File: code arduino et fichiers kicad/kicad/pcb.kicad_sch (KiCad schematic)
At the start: 34 parts, among them J1 Screw_Terminal_01x04, J2 Screw_Terminal_01x04, J3 Screw_Terminal_01x02, U1 LMC6482, U2 LMC6482, U3 LMC6482

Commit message: pcb yaddi yadda
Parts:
- removed LED1: LED_LEDCHIP-LED0805, LED_SMD:LED_0805_2012Metric_Pad1.15x1.40mm_HandSolder, symbol Arduino_MEGA_2560-Rev3:LED_LEDCHIP-LED0805
- added D4: LED, PCM_SparkFun-LED:LED_0603_1608Metric, symbol PCM_SparkFun-LED:LED
- added TP1, TP2, TP3: TestPoint, TestPoint:TestPoint_THTPad_D1.5mm_Drill0.7mm, symbol Connector:TestPoint
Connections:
- net GND: now also D4.1 (K)
- net T1 sortie: now also TP1.1
- net T2 sortie: now also TP2.1
- net T3 sortie: now also TP3.1
- net at R18.2: now also D4.2 (A)
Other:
- moved on the sheet: J1, J2, J3, R1, R10, R11, R12, R13, R14, R15, R18, R2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

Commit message: version tht pour pas trop haïr notre vie plus tard
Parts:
- removed J2: Screw_Terminal_01x04, Connector_JST:JST_XH_B4B-XH-A_1x04_P2.50mm_Vertical, symbol Connector:Screw_Terminal_01x04
- removed R1, R10, R15: 6.1K, Resistor_SMD:R_0805_2012Metric_Pad1.20x1.40mm_HandSolder, symbol Device:R
- removed digital1, digital2: Conn_01x18_Pin, Connector_PinHeader_2.54mm:PinHeader_1x18_P2.54mm_Vertical, symbol Connector:Conn_01x18_Pin
- added C16, C17, C18: 2 μF, Capacitor_THT:CP_Radial_D5.0mm_P2.50mm, symbol Device:C
- added RV1, RV2, RV3: R_Potentiometer_Trim, Library:trimpot, symbol Device:R_Potentiometer_Trim
- D4: footprint PCM_SparkFun-LED:LED_0603_1608Metric -> LED_THT:LED_D5.0mm
- R11, R12, R13, R14, R18, R2, R3, R4, R5, R6, R7, R8, R9: footprint Resistor_SMD:R_0805_2012Metric_Pad1.20x1.40mm_HandSolder -> Resistor_THT:R_Axial_DIN0207_L6.3mm_D2.5mm_P7.62mm_Horizontal
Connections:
- net +3.3V: no longer R18.1
- net +5V: now also R18.1
- net +8V: now also J3.2 (Pin_2); no longer J3.1 (Pin_1)
- net GND: now also J3.1 (Pin_1), RV1.3, RV2.3, RV3.3; no longer J3.2 (Pin_2)
- net T1 sortie: now also C16.2, RV1.2
- net T2 sortie: now also C17.2, RV2.2
- net T3 sortie: now also C18.2, RV3.2
- net pwmdroite: now also J1.3 (Pin_3)
- net at R2.2, U1.3 (+): now also C16.1, RV1.1
- net at R8.2, U2.3 (+): now also C17.1, RV2.1
- net at R13.2, U3.3 (+): now also C18.1, RV3.1
- no-connect marks 3 -> 1
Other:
- moved on the sheet: J1, J3, R11, R12, R13, R14, R6, R7, R8, R9, TH2, TH3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

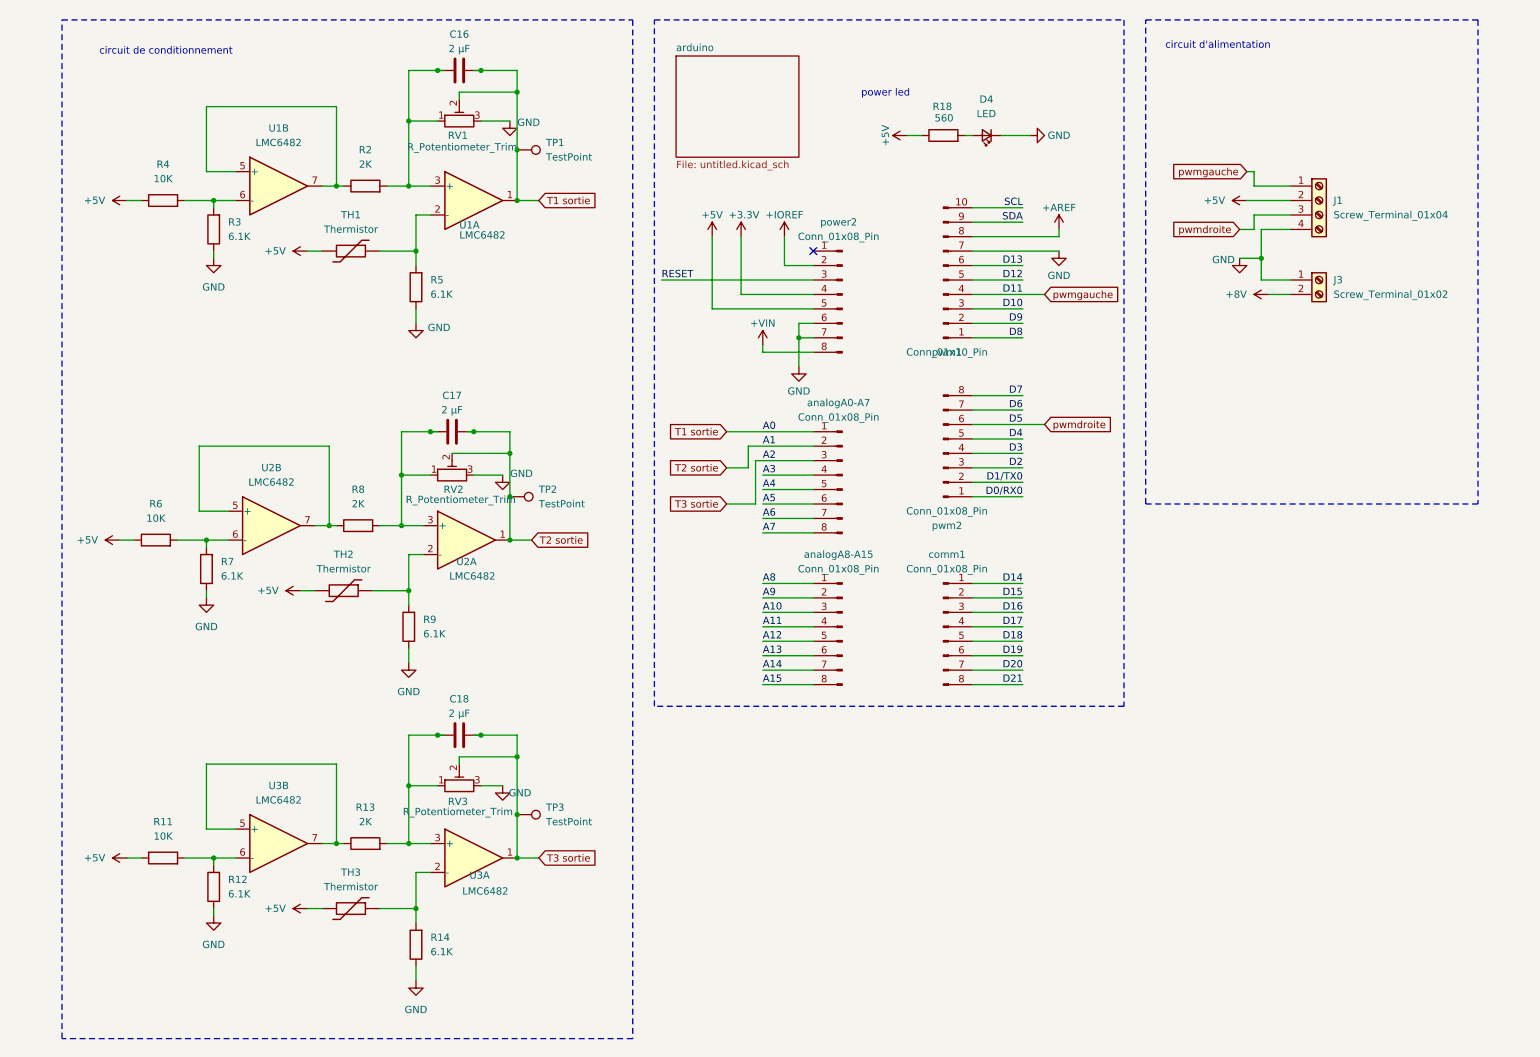
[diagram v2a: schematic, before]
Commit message: Changment connecteur pcb
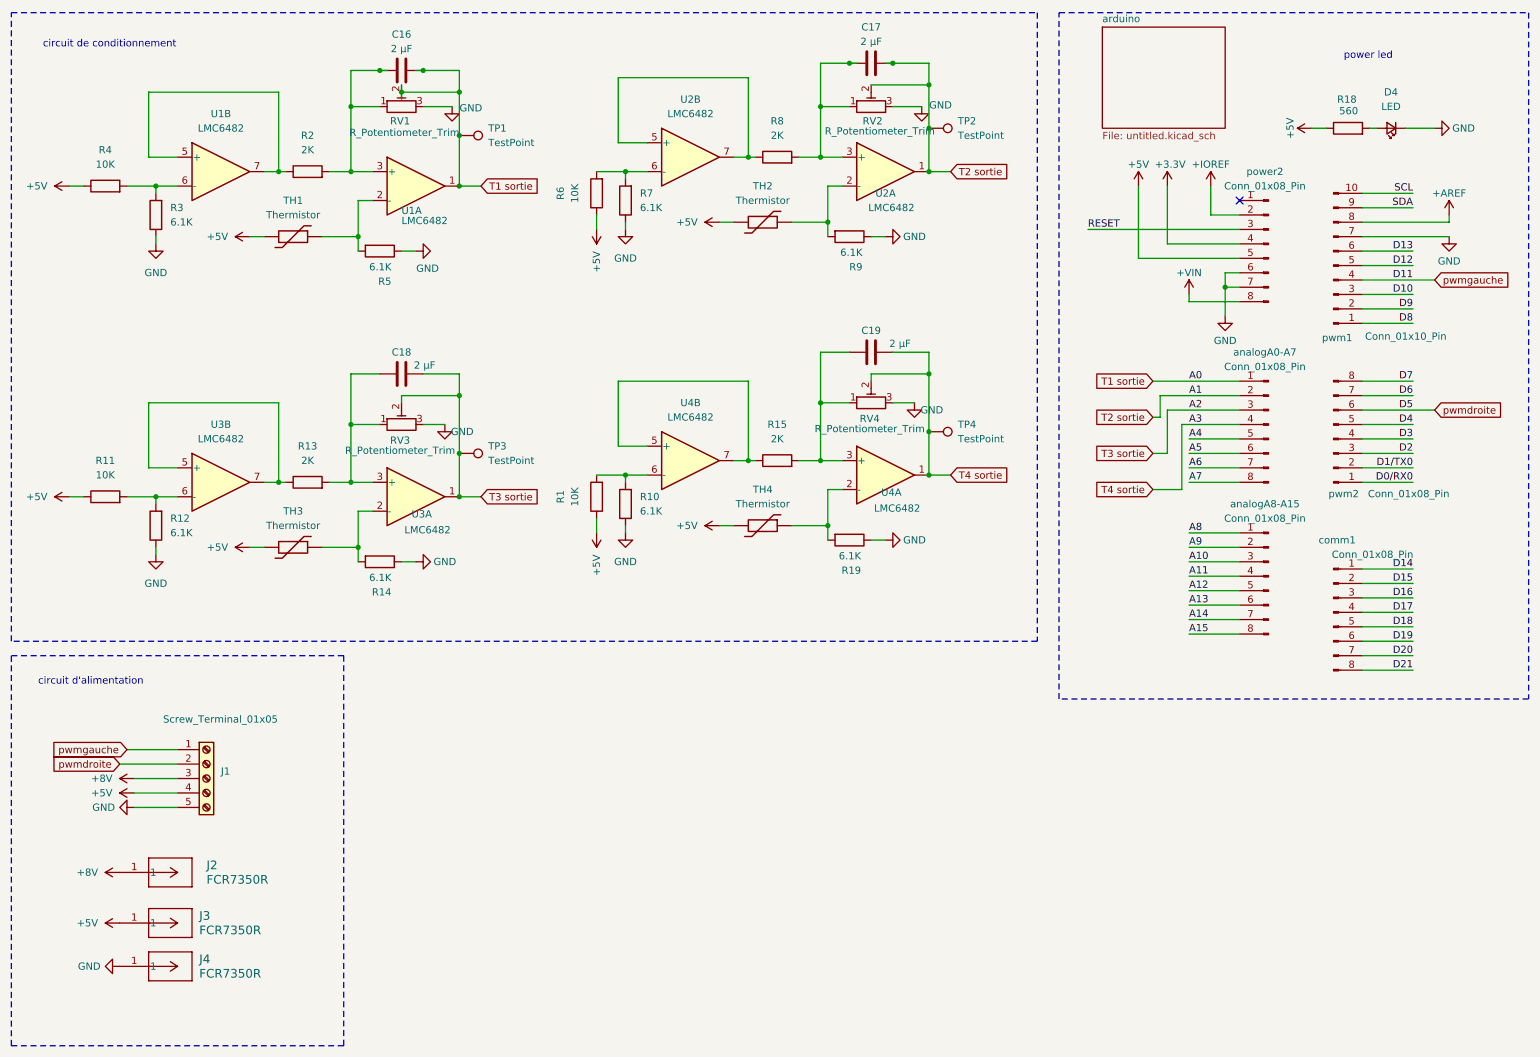
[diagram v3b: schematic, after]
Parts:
- removed J1: Screw_Terminal_01x04, Connector_JST:JST_XH_B4B-XH-A_1x04_P2.50mm_Vertical, symbol Connector:Screw_Terminal_01x04
- removed J3: Screw_Terminal_01x02, Connector_JST:JST_XH_B2B-XH-A_1x02_P2.50mm_Vertical, symbol Connector:Screw_Terminal_01x02
- added C19: 2 μF, Capacitor_THT:CP_Radial_D5.0mm_P2.50mm, symbol Device:C
- added J1: Screw_Terminal_01x05, Connector_JST:JST_XH_B5B-XH-A_1x05_P2.50mm_Vertical, symbol Connector:Screw_Terminal_01x05
- added J2, J3, J4: FCR7350R, CONN1_FCR7350R_CLF, symbol connecteur:FCR7350R
- added R1: 10K, Resistor_THT:R_Axial_DIN0207_L6.3mm_D2.5mm_P7.62mm_Horizontal, symbol Device:R
- added R10, R19: 6.1K, Resistor_THT:R_Axial_DIN0207_L6.3mm_D2.5mm_P7.62mm_Horizontal, symbol Device:R
- added R15: 2K, Resistor_THT:R_Axial_DIN0207_L6.3mm_D2.5mm_P7.62mm_Horizontal, symbol Device:R
- added RV4: R_Potentiometer_Trim, Library:trimpot, symbol Device:R_Potentiometer_Trim
- added TH4: Thermistor, Connector_JST:JST_XH_B2B-XH-A_1x02_P2.50mm_Vertical, symbol Device:Thermistor
- added TP4: TestPoint, TestPoint:TestPoint_THTPad_D1.5mm_Drill0.7mm, symbol Connector:TestPoint
- added U4: LMC6482, ampli op:LMC6482, symbol Amplifier_Operational:LMC6482
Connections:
- net +5V: now also J1.4 (Pin_4), J3.1, R1.1, TH4.2
- net +8V: now also J1.3 (Pin_3), J2.1
- net GND: now also J1.5 (Pin_5), J4.1, R10.1, R19.1, RV4.3
- net pwmdroite: now also J1.2 (Pin_2)
- net pwmgauche: now also J1.1 (Pin_1)
- net A3 renamed T4 sortie
- net T4 sortie: now also C19.2, RV4.2, TP4.1, U4.1
- new net: C19.1, R15.2, RV4.1, U4.3 (+)
- new net: R15.1, U4.5 (+), U4.7
- new net: R1.2, R10.2, U4.6 (-)
- new net: R19.2, TH4.1, U4.2 (-)
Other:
- moved on the sheet: C16, C17, C18, D4, R11, R12, R13, R14, R18, R2, R3, R4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

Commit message: Pcb quasi fini
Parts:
- C16, C17, C18, C19: footprint Capacitor_THT:CP_Radial_D5.0mm_P2.50mm -> Library:condensateur 1uF
- R1, R10, R11, R12, R13, R14, R15, R18, R19, R2, R3, R4, R5, R6, R7, R8, R9: footprint Resistor_THT:R_Axial_DIN0207_L6.3mm_D2.5mm_P7.62mm_Horizontal -> Library:Resistance SMT
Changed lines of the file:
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@@
 	)
 	(junction
-		(at 170.18 22.86)
-		(diameter 0)
-		(color 0 0 0 0)
-	)
-	(junction
 		(at 62.23 41.91)
 		(diameter 0)
@@
 	)
 	(junction
-		(at 80.01 24.13)
-		(diameter 0)
-		(color 0 0 0 0)
-	)
-	(junction
 		(at 74.93 96.52)
 		(diameter 0)
@@
 	)
 	(junction
-		(at 162.56 22.86)
-		(diameter 0)
-		(color 0 0 0 0)
-	)
-	(junction
 		(at 40.64 99.06)
 		(diameter 0)
@@
 	)
 	(junction
-		(at 87.63 24.13)
-		(diameter 0)
-		(color 0 0 0 0)
-	)
-	(junction
 		(at 74.93 30.48)
 		(diameter 0)
@@
 	(wire
 		(pts
-			(xy 86.36 24.13) (xy 87.63 24.13)
-		)
-		(stroke
-			(width 0)
-			(type default)
-		)
-	)
-	(wire
-		(pts
 			(xy 83.82 81.28) (xy 93.98 81.28)
 		)
@@
 	(wire
 		(pts
-			(xy 162.56 22.86) (xy 163.83 22.86)
+			(xy 157.48 22.86) (xy 162.56 22.86)
 		)
 		(stroke
@@
 	(wire
 		(pts
-			(xy 157.48 82.55) (xy 157.48 92.71)
+			(xy 170.18 22.86) (xy 176.53 22.86)
 		)
 		(stroke
@@
 	(wire
 		(pts
-			(xy 71.12 41.91) (xy 74.93 41.91)
+			(xy 157.48 82.55) (xy 157.48 92.71)
 		)
 		(stroke
@@
 	(wire
 		(pts
-			(xy 144.78 92.71) (xy 146.05 92.71)
+			(xy 71.12 41.91) (xy 74.93 41.91)
 		)
 		(stroke
@@
 	(wire
 		(pts
-			(xy 228.6 59.69) (xy 231.14 59.69)
+			(xy 144.78 92.71) (xy 146.05 92.71)
 		)
 		(stroke
@@
 	(wire
 		(pts
-			(xy 62.23 27.94) (xy 62.23 41.91)
+			(xy 228.6 59.69) (xy 231.14 59.69)
 		)
 		(stroke
@@
 	(wire
 		(pts
-			(xy 168.91 22.86) (xy 170.18 22.86)
+			(xy 62.23 27.94) (xy 62.23 41.91)
 		)
 		(stroke
@@
 	(wire
 		(pts
-			(xy 157.48 22.86) (xy 162.56 22.86)
-		)
-		(stroke
-			(width 0)
-			(type default)
-		)
-	)
-	(wire
-		(pts
 			(xy 220.98 97.79) (xy 220.98 86.36)
 		)
@@
 	(wire
 		(pts
-			(xy 118.11 52.07) (xy 118.11 49.53)
+			(xy 74.93 24.13) (xy 80.01 24.13)
 		)
 		(stroke
@@
 	(wire
 		(pts
-			(xy 175.26 30.48) (xy 170.18 30.48)
+			(xy 118.11 52.07) (xy 118.11 49.53)
 		)
 		(stroke
@@
 	(wire
 		(pts
-			(xy 74.93 24.13) (xy 80.01 24.13)
+			(xy 175.26 30.48) (xy 170.18 30.48)
 		)
 		(stroke
@@
 	(wire
 		(pts
-			(xy 80.01 24.13) (xy 81.28 24.13)
-		)
-		(stroke
-			(width 0)
-			(type default)
-		)
-	)
-	(wire
-		(pts
 			(xy 215.9 91.44) (xy 218.44 91.44)
 		)
@@
 	(wire
 		(pts
-			(xy 170.18 22.86) (xy 176.53 22.86)
-		)
-		(stroke
-			(width 0)
-			(type default)
-		)
-	)
-	(wire
-		(pts
 			(xy 118.11 95.25) (xy 123.19 95.25)
 		)
@@
 			)
 		)
-		(property "Footprint" "Capacitor_THT:CP_Radial_D5.0mm_P2.50mm"
+		(property "Footprint" "Library:condensateur 1uF"
 			(at 87.63 76.5048 0)
 			(effects
@@
 			)
 		)
-		(property "Footprint" "Resistor_THT:R_Axial_DIN0207_L6.3mm_D2.5mm_P7.62mm_Horizontal"
+		(property "Footprint" "Library:Resistance SMT"
 			(at 124.968 46.99 90)
 			(effects
@@
 			)
 		)
-		(property "Footprint" "Resistor_THT:R_Axial_DIN0207_L6.3mm_D2.5mm_P7.62mm_Horizontal"
+		(property "Footprint" "Library:Resistance SMT"
 			(at 42.418 104.14 90)
 			(effects
@@
 			)
 		)
-		(property "Footprint" "Capacitor_THT:CP_Radial_D5.0mm_P2.50mm"
+		(property "Footprint" "Library:condensateur 1uF"
 			(at 170.18 72.6948 0)
 			(effects
@@
 			)
 		)
-		(property "Footprint" "Resistor_THT:R_Axial_DIN0207_L6.3mm_D2.5mm_P7.62mm_Horizontal"
+		(property "Footprint" "Library:Resistance SMT"
 			(at 149.86 94.488 90)
 			(effects
@@
 			)
 		)
-		(property "Footprint" "Resistor_THT:R_Axial_DIN0207_L6.3mm_D2.5mm_P7.62mm_Horizontal"
+		(property "Footprint" "Library:Resistance SMT"
 			(at 119.888 99.06 90)
 			(effects
@@
 			)
 		)
-		(property "Footprint" "Resistor_THT:R_Axial_DIN0207_L6.3mm_D2.5mm_P7.62mm_Horizontal"
+		(property "Footprint" "Library:Resistance SMT"
 			(at 162.56 51.562 90)
 			(effects
@@
 			)
 		)
-		(property "Footprint" "Capacitor_THT:CP_Radial_D5.0mm_P2.50mm"
+		(property "Footprint" "Library:condensateur 1uF"
 			(at 170.18 21.8948 0)
 			(effects
@@
 			)
 		)
-		(property "Footprint" "Resistor_THT:R_Axial_DIN0207_L6.3mm_D2.5mm_P7.62mm_Horizontal"
+		(property "Footprint" "Library:Resistance SMT"
 			(at 124.968 100.33 90)
 			(effects
@@
 			)
 		)
-		(property "Footprint" "Resistor_THT:R_Axial_DIN0207_L6.3mm_D2.5mm_P7.62mm_Horizontal"
+		(property "Footprint" "Library:Resistance SMT"
 			(at 67.31 98.298 90)
 			(effects
@@
 			)
 		)
-		(property "Footprint" "Resistor_THT:R_Axial_DIN0207_L6.3mm_D2.5mm_P7.62mm_Horizontal"
+		(property "Footprint" "Library:Resistance SMT"
 			(at 31.75 46.228 90)
 			(effects
@@
 			)
 		)
-		(property "Footprint" "Resistor_THT:R_Axial_DIN0207_L6.3mm_D2.5mm_P7.62mm_Horizontal"
+		(property "Footprint" "Library:Resistance SMT"
 			(at 67.31 43.688 90)
 			(effects
@@
 			)
 		)
-		(property "Footprint" "Resistor_THT:R_Axial_DIN0207_L6.3mm_D2.5mm_P7.62mm_Horizontal"
+		(property "Footprint" "Library:Resistance SMT"
 			(at 80.01 54.102 90)
 			(effects
@@
 			)
 		)
-		(property "Footprint" "Resistor_THT:R_Axial_DIN0207_L6.3mm_D2.5mm_P7.62mm_Horizontal"
+		(property "Footprint" "Library:Resistance SMT"
 			(at 162.56 104.902 90)
 			(effects
@@
 			)
 		)
-		(property "Footprint" "Resistor_THT:R_Axial_DIN0207_L6.3mm_D2.5mm_P7.62mm_Horizontal"
+		(property "Footprint" "Library:Resistance SMT"
 			(at 250.19 36.068 90)
 			(effects
@@
 			)
 		)
-		(property "Footprint" "Resistor_THT:R_Axial_DIN0207_L6.3mm_D2.5mm_P7.62mm_Horizontal"
+		(property "Footprint" "Library:Resistance SMT"
 			(at 80.01 108.712 90)
 			(effects
@@
 			)
 		)
-		(property "Footprint" "Resistor_THT:R_Axial_DIN0207_L6.3mm_D2.5mm_P7.62mm_Horizontal"
+		(property "Footprint" "Library:Resistance SMT"
 			(at 119.888 45.72 90)
 			(effects
@@
 			)
 		)
-		(property "Footprint" "Resistor_THT:R_Axial_DIN0207_L6.3mm_D2.5mm_P7.62mm_Horizontal"
+		(property "Footprint" "Library:Resistance SMT"
 			(at 31.75 100.838 90)
 			(effects
@@
 			)
 		)
-		(property "Footprint" "Resistor_THT:R_Axial_DIN0207_L6.3mm_D2.5mm_P7.62mm_Horizontal"
+		(property "Footprint" "Library:Resistance SMT"
 			(at 42.418 49.53 90)
 			(effects
@@
 			)
 		)
-		(property "Footprint" "Capacitor_THT:CP_Radial_D5.0mm_P2.50mm"
+		(property "Footprint" "Library:condensateur 1uF"
 			(at 87.63 23.1648 0)
 			(effects
@@
 			)
 		)
-		(property "Footprint" "Resistor_THT:R_Axial_DIN0207_L6.3mm_D2.5mm_P7.62mm_Horizontal"
+		(property "Footprint" "Library:Resistance SMT"
 			(at 149.86 41.148 90)
 			(effects

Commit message: PCB partie 4, bom fini ?
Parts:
- C16, C17, C18, C19: value 2 μF -> 1 μF
- TH1, TH2, TH3, TH4: value Thermistor -> Screw_Terminal_01x02
- TP1, TP2, TP3, TP4: now left out of the parts list
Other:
- removed sheet arduino
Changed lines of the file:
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@@
 			)
 		)
-		(property "Value" "2 μF"
+		(property "Value" "1 μF"
 			(at 87.884 75.946 90)
 			(effects
@@
 			)
 		)
-		(property "Value" "2 μF"
+		(property "Value" "1 μF"
 			(at 171.45 72.136 90)
 			(effects
@@
 			)
 		)
-		(property "Value" "2 μF"
+		(property "Value" "1 μF"
 			(at 166.37 19.05 90)
 			(effects
@@
 			)
 		)
-		(property "Value" "Thermistor"
+		(property "Value" "Screw_Terminal_01x02"
 			(at 64.77 104.14 90)
 			(effects
@@
 		(unit 1)
 		(exclude_from_sim no)
-		(in_bom yes)
+		(in_bom no)
 		(on_board yes)
 		(dnp no)
@@
 		(unit 1)
 		(exclude_from_sim no)
-		(in_bom yes)
+		(in_bom no)
 		(on_board yes)
 		(dnp no)
@@
 			)
 		)
-		(property "Value" "Thermistor"
+		(property "Value" "Screw_Terminal_01x02"
 			(at 147.32 100.33 90)
 			(effects
@@
 		(unit 1)
 		(exclude_from_sim no)
-		(in_bom yes)
+		(in_bom no)
 		(on_board yes)
 		(dnp no)
@@
 			)
 		)
-		(property "Value" "2 μF"
+		(property "Value" "1 μF"
 			(at 83.82 20.32 90)
 			(effects
@@
 		(unit 1)
 		(exclude_from_sim no)
-		(in_bom yes)
+		(in_bom no)
 		(on_board yes)
 		(dnp no)
@@
 			)
 		)
-		(property "Value" "Thermistor"
+		(property "Value" "Screw_Terminal_01x02"
 			(at 64.77 49.53 90)
 			(effects
@@
 			)
 		)
-		(property "Value" "Thermistor"
+		(property "Value" "Screw_Terminal_01x02"
 			(at 147.32 46.99 90)
 			(effects
@@
 				)
 			)
-		)
-	)
-	(sheet
-		(at 207.01 16.51)
-		(size 21.59 17.78)
-		(exclude_from_sim no)
-		(in_bom yes)
-		(on_board yes)
-		(dnp no)
-		(fields_autoplaced yes)
-		(stroke
-			(width 0.1524)
-			(type solid)
-		)
-		(fill
-			(color 0 0 0 0.0000)
-		)
-		(property "Sheetname" "arduino"
-			(at 207.01 15.7984 0)
-			(effects
-				(font
-					(size 1.27 1.27)
-				)
-				(justify left bottom)
-			)
-		)
-		(property "Sheetfile" "untitled.kicad_sch"
-			(at 207.01 34.8746 0)
-			(effects
-				(font
-					(size 1.27 1.27)
-				)
-				(justify left top)
-			)
-		)
-		(instances
-			(project "pcb"
-				(path "/08655c7e-db3e-4a36-827c-446c5903f8cb"
-					(page "2")
-				)
-			)

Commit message: Changements connecteurs
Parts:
- removed J1: Screw_Terminal_01x05, Connector_JST:JST_XH_B5B-XH-A_1x05_P2.50mm_Vertical, symbol Connector:Screw_Terminal_01x05
- removed J2, J3, J4: FCR7350R, CONN1_FCR7350R_CLF, symbol connecteur:FCR7350R
- added J1: Screw_Terminal_01x04, Connector_JST:JST_PH_B4B-PH-K_1x04_P2.00mm_Vertical, symbol Connector:Screw_Terminal_01x04
- added J2: Screw_Terminal_01x02, Connector_JST:JST_PH_B2B-PH-K_1x02_P2.00mm_Vertical, symbol Connector:Screw_Terminal_01x02
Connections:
- net +5V: now also J1.4 (Pin_4), J2.2 (Pin_2)
- net GND: now also J1.3 (Pin_3), J2.1 (Pin_1)
- net pwmdroite: now also J1.2 (Pin_2)
- net pwmgauche: now also J1.1 (Pin_1)
